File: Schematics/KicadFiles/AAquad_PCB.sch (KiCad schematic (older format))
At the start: 38 parts, among them IC1 L3GD20H, J1 programmer, Q1 BSS138, Q2 BSS138, U1 ATMEGA328-AU, U2 LIS3DHTR

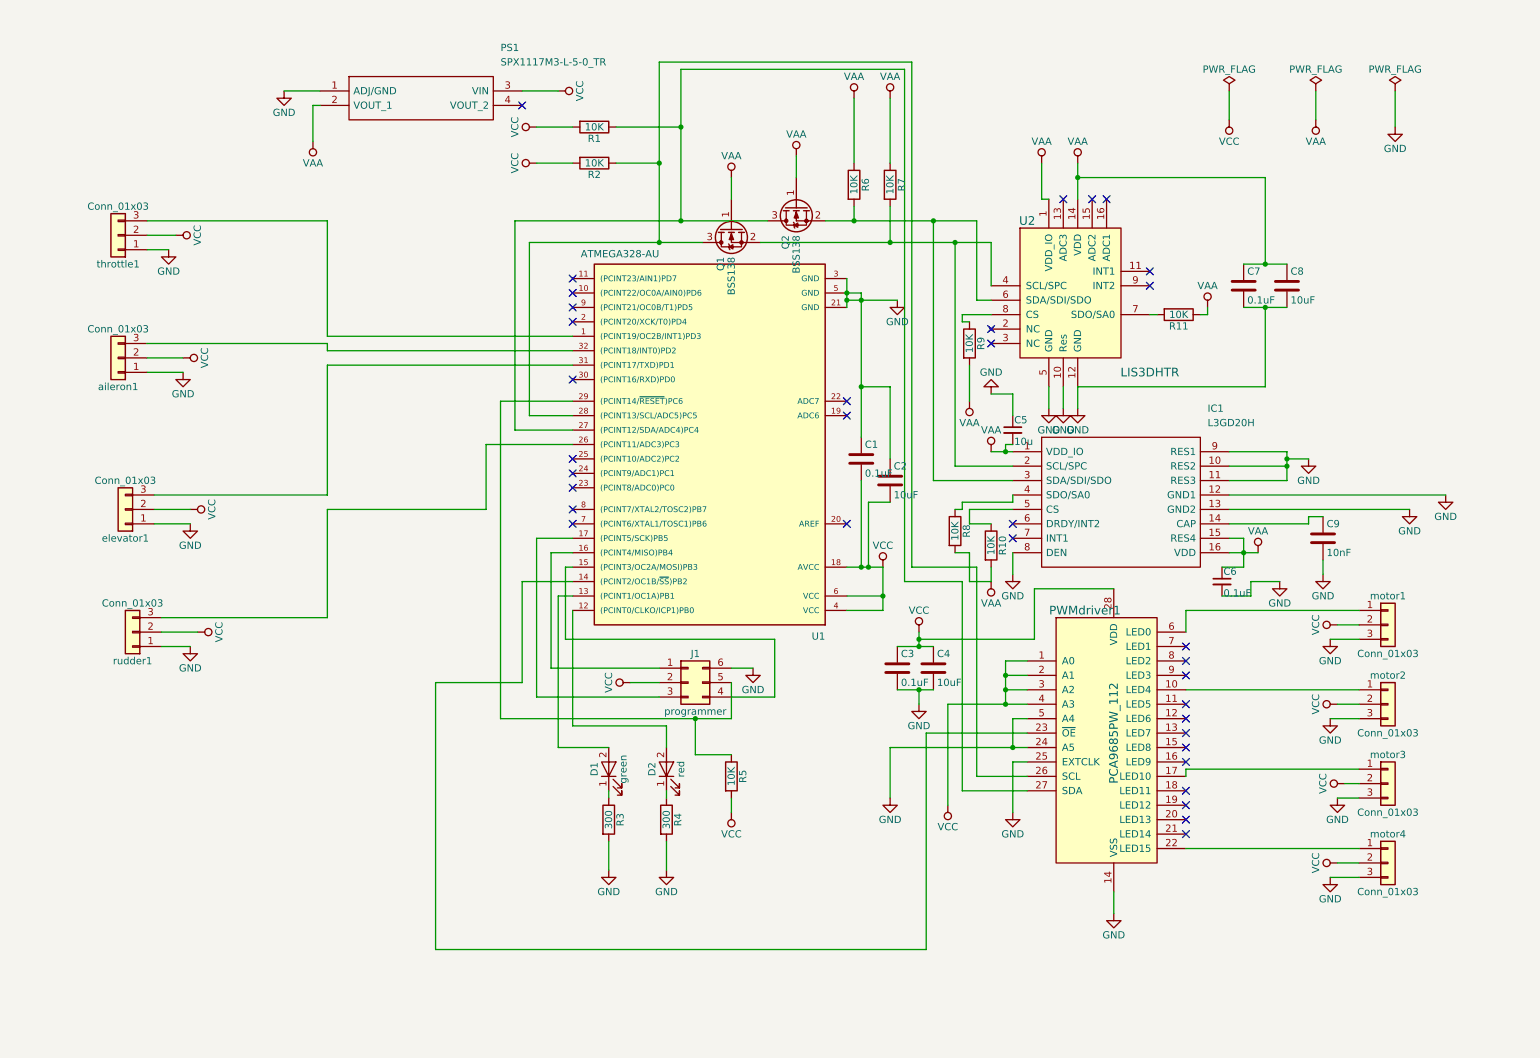
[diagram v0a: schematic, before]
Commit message: PCB redesign to include IMU, barometer, and various other features
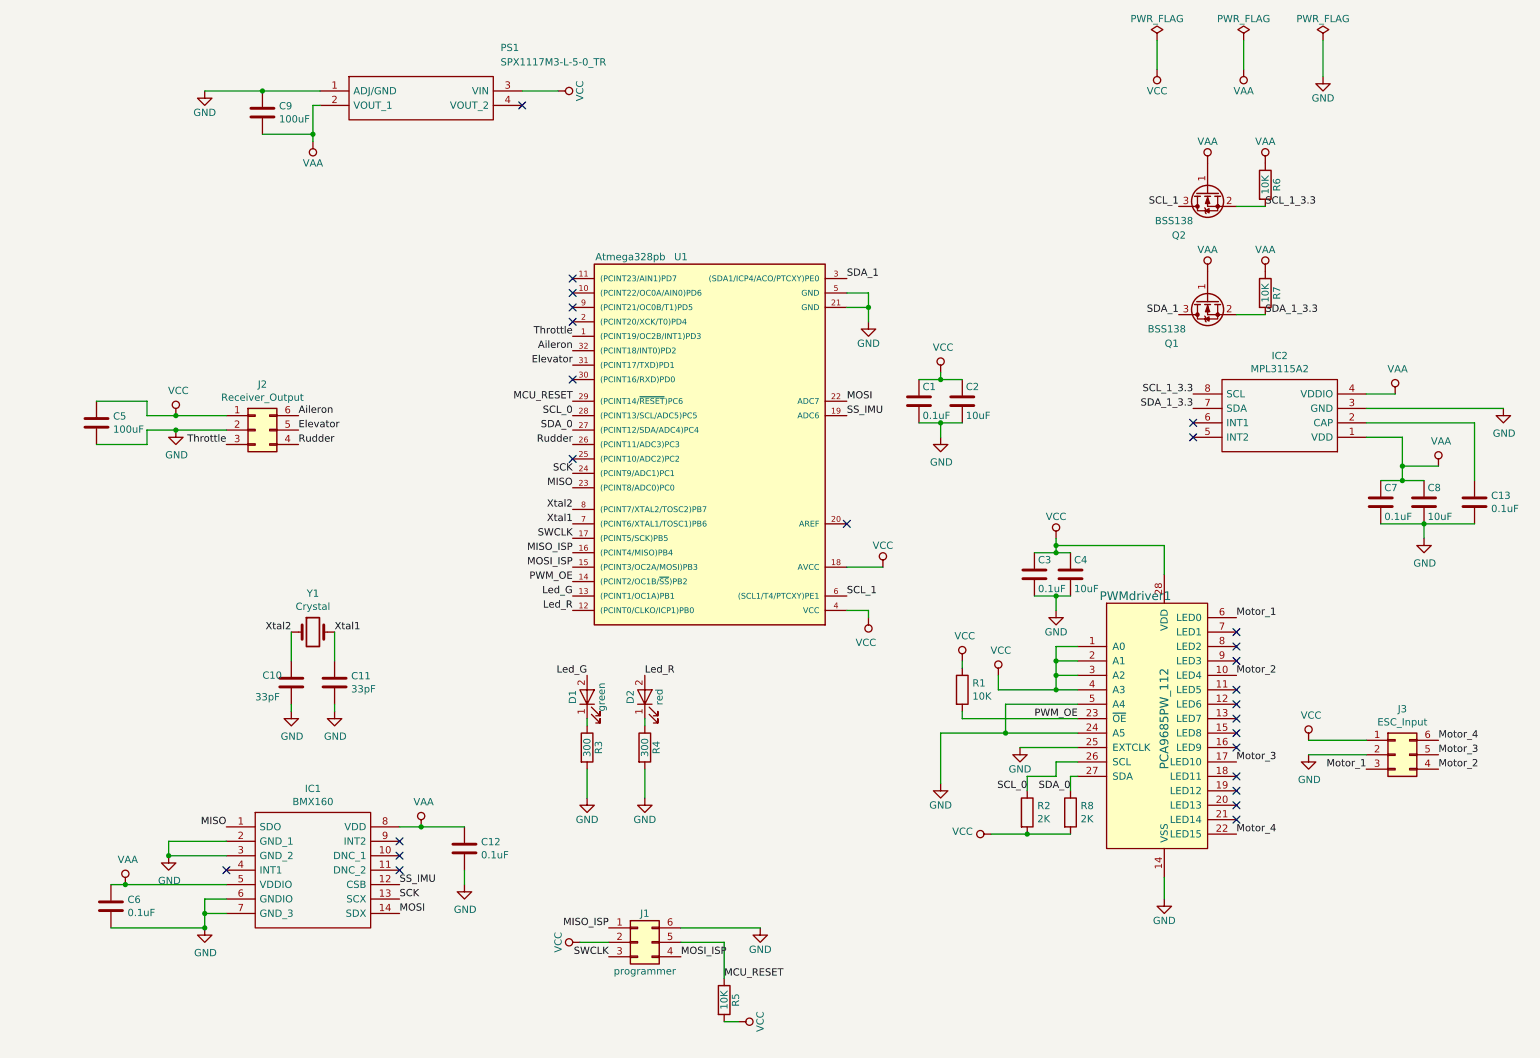
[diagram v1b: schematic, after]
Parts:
- removed C5: 10u, Capacitors_SMD:C_0805_HandSoldering, symbol AAquad_PCB-rescue:C_Small
- removed C6: 0.1uF, Capacitors_SMD:C_0805_HandSoldering, symbol AAquad_PCB-rescue:C_Small
- removed C9: 10nF, Capacitors_SMD:C_0805_HandSoldering, symbol AAquad_PCB-rescue:C
- removed IC1: L3GD20H, footprints:L3gd20h, symbol AAquad_PCB-rescue:L3GD20H-RESCUE-AAquad_PCB
- removed R1, R10, R11, R2, R8, R9: 10K, Resistors_SMD:R_0805_HandSoldering, symbol AAquad_PCB-rescue:R
- removed U1: ATMEGA328-AU, Housings_QFP:TQFP-32_7x7mm_Pitch0.8mm, symbol AAquad_PCB-rescue:ATMEGA328-AU
- removed U2: LIS3DHTR, footprints:Lis3dh, symbol AAquad_PCB-rescue:LIS3DHTR-RESCUE-AAquad_PCB
- removed aileron1, elevator1, motor1, motor2, motor3, motor4, rudder1, throttle1: Conn_01x03, Pin_Headers:Pin_Header_Straight_1x03_Pitch2.54mm, symbol AAquad_PCB-rescue:Conn_01x03
- added C10, C11: 33pF, Capacitor_SMD:C_0402_1005Metric, symbol Device:C
- added C12, C13, C6: 0.1uF, Capacitors_SMD:C_0805, symbol Device:C
- added C5, C9: 100uF, Capacitor_SMD:C_1206_3216Metric, symbol Device:C
- added IC1: BMX160, sensors:bmx160, symbol BMX160:BMX160
- added IC2: MPL3115A2, sensors:MPL3115A2, symbol MPL3115A2:MPL3115A2
- added J2: Receiver_Output, Connector_PinHeader_2.54mm:PinHeader_2x03_P2.54mm_Vertical, symbol Connector_Generic:Conn_02x03_Counter_Clockwise
- added J3: ESC_Input, Connector_PinHeader_2.54mm:PinHeader_2x03_P2.54mm_Vertical, symbol Connector_Generic:Conn_02x03_Counter_Clockwise
- added R1: 10K, Resistor_SMD:R_0805_2012Metric, symbol Device:R
- added R2, R8: 2K, Resistor_SMD:R_0805_2012Metric, symbol Device:R
- added U1: Atmega328pb, microcontrollers:ATMEGA328PB-ANR, symbol Misc:Atmega328pb
- added Y1: Crystal, Crystals:Crystal_SMD_7050-2pin_7.0x5.0mm, symbol Device:Crystal
- C1, C2, C3, C4, C7, C8: footprint Capacitors_SMD:C_0805_HandSoldering -> Capacitors_SMD:C_0805
- J1: footprint Pin_Headers:Pin_Header_Straight_2x03_Pitch2.54mm -> Connector_PinHeader_2.54mm:PinHeader_2x03_P2.54mm_Vertical
- R3, R4, R5, R6, R7: footprint Resistors_SMD:R_0805_HandSoldering -> Resistor_SMD:R_0805_2012Metric
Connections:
- net GND: now also C1.2, C2.2, C10.2, C11.2, C12.1, C13.2, C5.2, C6.1, C9.1, IC1.2 (GND_1), IC1.3 (GND_2), IC1.6 (GNDIO), IC1.7 (GND_3), IC2.3 (GND), J2.2 (Pin_2), J3.2 (Pin_2), U1.21 (GND), U1.5 (GND); no longer C1.1, C2.1
- net VAA: now also C12.2, C6.2, C9.2, IC1.5 (VDDIO), IC1.8 (VDD), IC2.1 (VDD), IC2.4 (VDDIO)
- net VCC: now also C1.1, C2.1, C5.1, J2.1 (Pin_1), J3.1 (Pin_1), R1.1, R2.2, R8.2, U1.18 (AVCC), U1.4 (VCC); no longer C1.2, C2.2
- net Led_R: now reaches D2.2 (A)
- net Led_R: now also U1.12 ((PCINT0/CLKO/ICP1)PB0)
- net Led_G: now reaches D1.2 (A)
- net Led_G: now also U1.13 ((PCINT1/OC1A)PB1)
- net PWM_OE: now reaches PWMdriver1.23 (~OE)
- net PWM_OE: now also R1.2, U1.14 ((PCINT2/OC1B/~SS~)PB2)
- net MOSI_ISP: now reaches J1.4 (Pin_4)
- net MOSI_ISP: now also U1.15 ((PCINT3/OC2A/MOSI)PB3)
- net MISO_ISP: now reaches J1.1 (Pin_1)
- net MISO_ISP: now also U1.16 ((PCINT4/MISO)PB4)
- net SWCLK: now reaches J1.3 (Pin_3)
- net SWCLK: now also U1.17 ((PCINT5/SCK)PB5)
- net SCL_1: now reaches Q2.3 (D)
- net SCL_1: now also U1.6 ((SCL1/T4/PTCXY)PE1); no longer PWMdriver1.27 (SDA)
- net SCL_0: now reaches PWMdriver1.26 (SCL)
- net SCL_0: now also R2.1, U1.28 ((PCINT13/SCL/ADC5)PC5); no longer Q1.3 (D)
- net MCU_RESET: now reaches J1.5 (Pin_5), R5.1
- net MCU_RESET: now also U1.29 ((PCINT14/~RESET~)PC6)
- net Motor_1: now reaches PWMdriver1.6 (LED0)
- net Motor_1: now also J3.3 (Pin_3)
- net Motor_2: now reaches PWMdriver1.10 (LED4)
- net Motor_2: now also J3.4 (Pin_4)
- net Motor_3: now reaches PWMdriver1.17 (LED10)
- net Motor_3: now also J3.5 (Pin_5)
- net Motor_4: now reaches PWMdriver1.22 (LED15)
- net Motor_4: now also J3.6 (Pin_6)
- net SDA_1_3.3: now reaches Q1.2 (S), R7.2
- net SDA_1_3.3: now also IC2.7 (SDA)
- net SCL_1_3.3: now reaches Q2.2 (S), R6.2
- net SCL_1_3.3: now also IC2.8 (SCL)
- new net: C13.1, IC2.2 (CAP)
- new net Aileron: J2.6 (Pin_6), U1.32 ((PCINT18/INT0)PD2)
- new net Elevator: J2.5 (Pin_5), U1.31 ((PCINT17/TXD)PD1)
- new net MISO: IC1.1 (SDO), U1.23 ((PCINT8/ADC0)PC0)
- new net MOSI: IC1.14 (SDX), U1.22 (ADC7)
- new net Rudder: J2.4 (Pin_4), U1.26 ((PCINT11/ADC3)PC3)
- new net SCK: IC1.13 (SCX), U1.24 ((PCINT9/ADC1)PC1)
- new net SDA_0: PWMdriver1.27 (SDA), R8.1, U1.27 ((PCINT12/SDA/ADC4)PC4)
- new net SDA_1: Q1.3 (D), U1.3 ((SDA1/ICP4/ACO/PTCXY)PE0)
- new net SS_IMU: IC1.12 (CSB), U1.19 (ADC6)
- new net Throttle: J2.3 (Pin_3), U1.1 ((PCINT19/OC2B/INT1)PD3)
- new net Xtal1: C11.1, U1.7 ((PCINT6/XTAL1/TOSC1)PB6), Y1.2
- new net Xtal2: C10.1, U1.8 ((PCINT7/XTAL2/TOSC2)PB7), Y1.1
- no-connect marks 35 -> 26
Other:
- moved on the sheet: C1, C2, C3, C4, C7, C8, D1, D2, J1, PWMdriver1, Q1, Q2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

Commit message: Completed PCB redesign
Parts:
- added C14, C15, C16, C17: 10uF, Capacitor_SMD:C_0805_2012Metric, symbol Device:C
- added IC3, IC4, IC5, IC6: levelShifter, levelShifters:74LVC1T45GW_125, symbol 74LVC1T45GW_125:74LVC1T45GW,125
- added J4: ultrasonic, Connector_PinHeader_2.54mm:PinHeader_2x02_P2.54mm_Vertical, symbol Connector_Generic:Conn_02x02_Counter_Clockwise
- renumbered PWMdriver1 to U2
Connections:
- net Aileron: now also J2.4 (Pin_4); no longer J2.6 (Pin_6)
- net GND: now also C14.2, C15.2, C16.2, C17.2, IC3.2, IC4.2, IC5.2, IC5.5, IC6.2, J4.2 (Pin_2)
- net Led_G: now also U1.10 ((PCINT22/OC0A/AIN0)PD6); no longer U1.13 ((PCINT1/OC1A)PB1)
- net Led_R: now also U1.9 ((PCINT21/OC0B/T1)PD5); no longer U1.12 ((PCINT0/CLKO/ICP1)PB0)
- net MISO: now also IC5.3; no longer IC1.1 (SDO)
- net MOSI: now also IC4.3; no longer IC1.14 (SDX)
- net Motor_1: now also J3.6 (Pin_6); no longer J3.3 (Pin_3)
- net Motor_2: now also J3.5 (Pin_5), U2.7 (LED1); no longer J3.4 (Pin_4), U2.10 (LED4)
- net Motor_3: now also J3.3 (Pin_3), U2.8 (LED2); no longer J3.5 (Pin_5), U2.17 (LED10)
- net Motor_4: now also J3.4 (Pin_4), U2.9 (LED3); no longer J3.6 (Pin_6), U2.22 (LED15)
- net PWM_OE: now also U1.25 ((PCINT10/ADC2)PC2); no longer U1.14 ((PCINT2/OC1B/~SS~)PB2)
- net Rudder: now also J2.6 (Pin_6); no longer J2.4 (Pin_4)
- net SCK: now also IC3.3; no longer IC1.13 (SCX)
- net SS_IMU: now also IC6.3; no longer IC1.12 (CSB)
- net VAA: now also IC3.6, IC4.6, IC5.6, IC6.6
- net VCC: now also C14.1, C15.1, C16.1, C17.1, IC3.1, IC3.5, IC4.1, IC4.5, IC5.1, IC6.1, IC6.5, J4.1 (Pin_1)
- new net MISO_3.3: IC1.1 (SDO), IC5.4
- new net MOSI_3.3: IC1.14 (SDX), IC4.4
- new net SCK_3.3: IC1.13 (SCX), IC3.4
- new net SS_IMU_3.3: IC1.12 (CSB), IC6.4
- new net Ultrasonic_Echo: J4.4 (Pin_4), U1.13 ((PCINT1/OC1A)PB1)
- new net Ultrasonic_Trig: J4.3 (Pin_3), U1.12 ((PCINT0/CLKO/ICP1)PB0)
- no-connect marks 26 -> 24
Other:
- moved on the sheet: C10, C11, C12, C6, D1, D2, IC1, R3, R4, Y1
